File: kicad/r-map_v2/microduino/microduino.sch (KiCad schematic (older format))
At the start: 15 parts, among them P1 CONN_01X02, P2 CONN_RELE_BOARD, P3 CONN_01X05, P4 CONFIG, P5 USB_OTG, U1 Microduino, U2 ESDA6V1-5SC6, U3 LP2985LV, U4 TMP275

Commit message: Add files from last commit on sourceforge
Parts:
- removed R1: 1K0, w_smd_resistors:r_1206, symbol R
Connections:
- net GND: now also U4.5 (A2)
- net SCL: now reaches P3.2 (P2), U1.12 (A5), U2.5 (IO4), U4.2 (SCL)
- net SDA: now reaches P3.3 (P3), U1.13 (A4), U2.4 (IO3), U4.1 (SDA)
- net SCK: now reaches U1.19 (D13)
- net MISO: now reaches U1.20 (D12)
- net MOSI: now reaches U1.21 (D11)
- net CS-NRF24: now reaches U1.22 (D10)
- net CE-NRF24: now reaches U1.23 (D9)
- net CS-ENC28J60: now reaches P4.2 (P2), U1.24 (D8)
- net +3.3V: now reaches C3.1, D1.2 (A), P3.5 (P5), U1.26 (3V3), U3.5 (VOUT), U4.8 (Vcc)
- net +5V: now reaches C1.1, P1.1 (P1), P2.6 (P6), P3.1 (P1), P5.1 (VCC), U1.27 (5V), U3.1 (VIN), U3.3 (ON/OFF)
- net TX1: now reaches P2.4 (P4), U1.6 (D3)
- net INT-28J60: now reaches P2.5 (P5), U1.7 (D2)
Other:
- moved on the sheet: P4
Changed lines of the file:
@@
 	-1   0    0    1
 $EndComp
-Text Label 6950 4300 1    60   ~ 0
+Text Label 7150 4250 1    60   ~ 0
 GND
-Text Label 3600 4650 2    60   ~ 0
+Text Label 3700 4500 2    60   ~ 0
 Vcc_RELE
 NoConn ~ 5050 5200
@@
 	1    0    0    -1
 $EndComp
-$Comp
-L R R1
-U 1 1 54900F55
-P 8300 3550
-F 0 "R1" V 8380 3550 40  0000 C CNN
-F 1 "1K0" V 8307 3551 40  0000 C CNN
-F 2 "w_smd_resistors:r_1206" V 8230 3550 30  0001 C CNN
-F 3 "" H 8300 3550 30  0000 C CNN
-	1    8300 3550
-	1    0    0    -1
-$EndComp
 NoConn ~ 8200 3450
 $Comp
 L CONN_02X01 P4
 U 1 1 54837A8A
-P 7000 4750
-F 0 "P4" H 7000 4600 50  0000 C CNN
-F 1 "CONFIG" H 7000 4650 50  0000 C CNN
-F 2 "w_pin_strip:pin_strip_2" H 7000 3550 60  0001 C CNN
-F 3 "" H 7000 3550 60  0000 C CNN
-	1    7000 4750
+P 7150 4750
+F 0 "P4" H 7150 4600 50  0000 C CNN
+F 1 "CONFIG" H 7150 4650 50  0000 C CNN
+F 2 "w_pin_strip:pin_strip_2" H 7150 3550 60  0001 C CNN
+F 3 "" H 7150 3550 60  0000 C CNN
+	1    7150 4750
 	0    1    1    0
 $EndComp
@@
 NoConn ~ 5050 4600
 Wire Wire Line
-	4100 5300 5050 5300
-Wire Wire Line
-	5950 3850 5400 3850
+	4100 5300 4800 5300
+Wire Wire Line
+	4800 5300 5050 5300
+Wire Wire Line
+	5950 3850 5650 3850
+Wire Wire Line
+	5650 3850 5400 3850
 Wire Wire Line
 	5650 3850 5650 4100
 Wire Wire Line
-	4200 3000 7000 3000
-Wire Wire Line
-	6150 2850 6150 3650
+	4200 3000 6050 3000
+Wire Wire Line
+	6050 3000 7150 3000
+Wire Wire Line
+	6150 2850 6150 2900
+Wire Wire Line
+	6150 2900 6150 3650
 Wire Wire Line
 	6600 5200 6600 3650
@@
 	6600 5400 6600 5300
 Wire Wire Line
-	3700 5400 6600 5400
+	3700 5400 4050 5400
+Wire Wire Line
+	4050 5400 6600 5400
 Wire Wire Line
 	3700 5400 3700 4500
@@
 	4100 4500 4100 4600
 Wire Wire Line
-	5950 2850 5950 3850
-Wire Wire Line
-	5850 3650 5850 2850
+	5950 2850 5950 3250
+Wire Wire Line
+	5950 3250 5950 3850
+Wire Wire Line
+	5850 3650 5850 3100
+Wire Wire Line
+	5850 3100 5850 2850
 Wire Wire Line
 	6050 3000 6050 2850
@@
 	5750 3450 6700 3450
 Wire Wire Line
-	6700 3450 6700 5300
+	6700 5300 6700 3450
 Connection ~ 6600 5300
 Wire Wire Line
 	6600 3650 6150 3650
 Wire Wire Line
-	5400 3650 5850 3650
+	5400 3650 5550 3650
+Wire Wire Line
+	5550 3650 5850 3650
 Connection ~ 5550 3650
 Connection ~ 5650 3850
@@
 	4050 7200 4050 6950
 Wire Wire Line
-	2750 7200 6550 7200
+	2750 7200 3250 7200
+Wire Wire Line
+	3250 7200 3700 7200
+Wire Wire Line
+	3700 7200 4050 7200
+Wire Wire Line
+	4050 7200 4450 7200
+Wire Wire Line
+	4450 7200 5450 7200
+Wire Wire Line
+	5450 7200 6350 7200
+Wire Wire Line
+	6350 7200 6550 7200
 Wire Wire Line
 	6550 7200 6550 6950
 Wire Wire Line
-	5450 7100 5450 7300
+	5450 7100 5450 7200
+Wire Wire Line
+	5450 7200 5450 7300
 Connection ~ 5450 7200
 Wire Wire Line
-	6550 5200 6550 6650
-Wire Wire Line
-	4050 5400 4050 6650
-Wire Wire Line
-	2750 6100 4650 6100
+	6550 5200 6550 6100
+Wire Wire Line
+	6550 6100 6550 6650
+Wire Wire Line
+	4050 5400 4050 6100
+Wire Wire Line
+	4050 6100 4050 6300
+Wire Wire Line
+	4050 6300 4050 6650
+Wire Wire Line
+	2750 6100 3250 6100
+Wire Wire Line
+	3250 6100 3700 6100
+Wire Wire Line
+	3700 6100 4050 6100
+Wire Wire Line
+	4050 6100 4650 6100
 Wire Wire Line
 	4050 6300 4650 6300
 Connection ~ 4050 6300
 Wire Wire Line
-	6250 6100 6550 6100
+	6250 6100 6350 6100
+Wire Wire Line
+	6350 6100 6550 6100
 Connection ~ 6550 5200
 Connection ~ 4050 7200
@@
 Connection ~ 5950 3250
 Wire Wire Line
-	7000 3000 7000 4500
-Wire Wire Line
-	8400 3950 7000 3950
+	7150 3000 7150 3950
+Wire Wire Line
+	7150 3950 7150 4500
+Wire Wire Line
+	8400 3950 7700 3950
+Wire Wire Line
+	7700 3950 7150 3950
 Connection ~ 6050 3000
 Wire Wire Line
@@
 	8200 3000 8400 3000
 Wire Wire Line
-	8400 3000 8400 3950
+	8400 3000 8400 3100
+Wire Wire Line
+	8400 3100 8400 3200
+Wire Wire Line
+	8400 3200 8400 3950
 Connection ~ 7700 3950
 Wire Wire Line
@@
 Connection ~ 8400 3100
 Wire Wire Line
-	8200 3200 8300 3200
-Wire Wire Line
-	8300 3200 8300 3400
-Wire Wire Line
-	6450 5000 7000 5000
-Connection ~ 7000 3950
+	8200 3200 8400 3200
+Wire Wire Line
+	6450 5000 7150 5000
+Connection ~ 7150 3950
 Connection ~ 4050 5400
 Wire Wire Line
@@
 Connection ~ 4800 5300
 Wire Wire Line
-	6450 5200 6600 5200
-Wire Wire Line
-	6700 5300 6450 5300
-Wire Wire Line
-	7700 3850 7700 4100
-Connection ~ 8300 3950
-Wire Wire Line
-	8300 3700 8300 3950
+	6450 5200 6550 5200
+Wire Wire Line
+	6550 5200 6600 5200
+Wire Wire Line
+	6450 5300 6600 5300
+Wire Wire Line
+	6600 5300 6700 5300
+Wire Wire Line
+	7700 3850 7700 3950
+Wire Wire Line
+	7700 3950 7700 4100
 NoConn ~ 2750 6400
 $Comp
@@
 	6350 7050 6350 7200
 Connection ~ 6350 7200
+Text Label 5650 3650 0    60   ~ 0
+SCL
+Text Label 5750 3850 0    60   ~ 0
+SDA
+Connection ~ 8400 3200
+Text Label 6700 2900 0    60   ~ 0
++3.3V
+Text Label 6350 3450 0    60   ~ 0
++5V
+Text Label 4350 6100 0    60   ~ 0
+VIN
+Text Label 6450 4500 0    60   ~ 0
+SCK
+Text Label 6450 4600 0    60   ~ 0
+MISO
+Text Label 6450 4700 0    60   ~ 0
+MOSI
+Text Label 6450 5000 0    60   ~ 0
+CS-ENC28J60
+Text Label 4250 4700 0    60   ~ 0
+INT-28J60
+Text Label 6450 4900 0    60   ~ 0
+CE-NRF24
+Text Label 6450 4800 0    60   ~ 0
+CS-NRF24
+Text Label 4800 4700 0    60   ~ 0
+RX1
+Text Label 4800 4800 0    60   ~ 0
+TX1
 $EndSCHEMATC

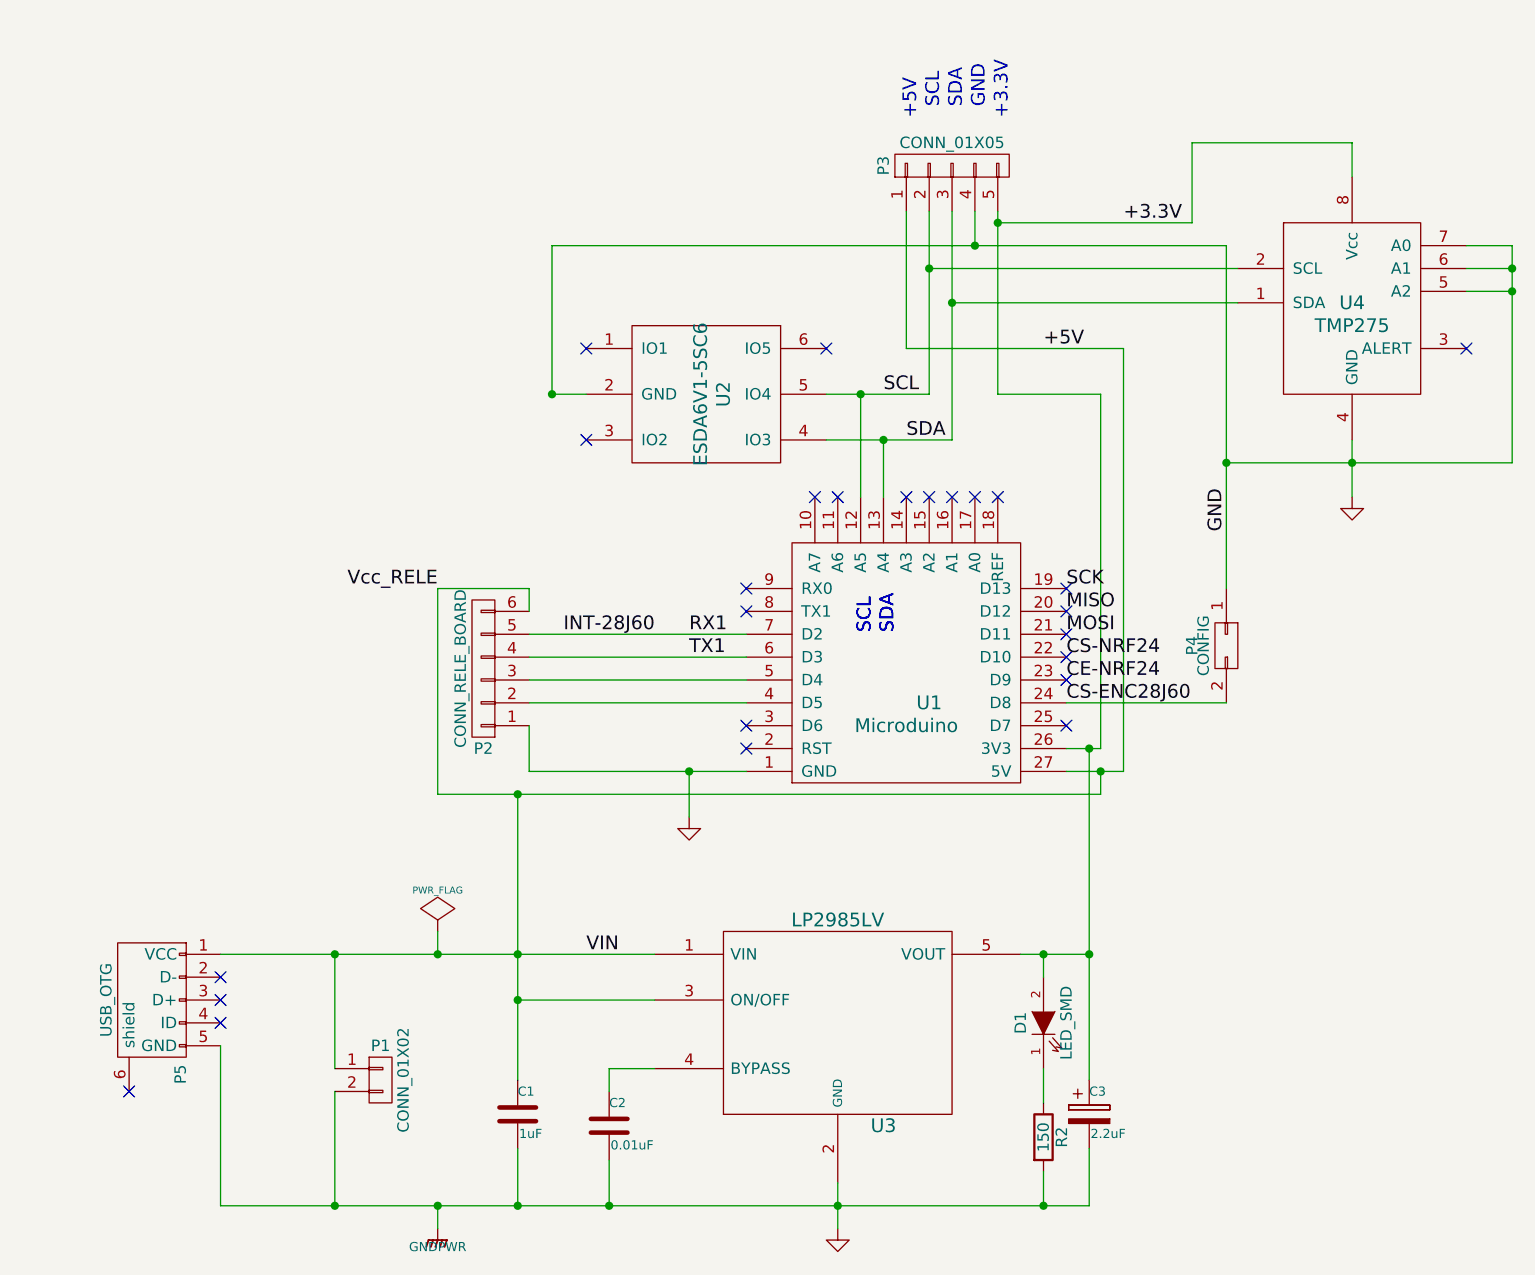
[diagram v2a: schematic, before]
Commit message: Modifiche a schema elettrico su modulo bluethoot, modificate connessioni per seriale 1. Modulo stima-i2c modificati pin per rele' e aggiunte connessioni esd su alimentazione. Rigenerati pcb.
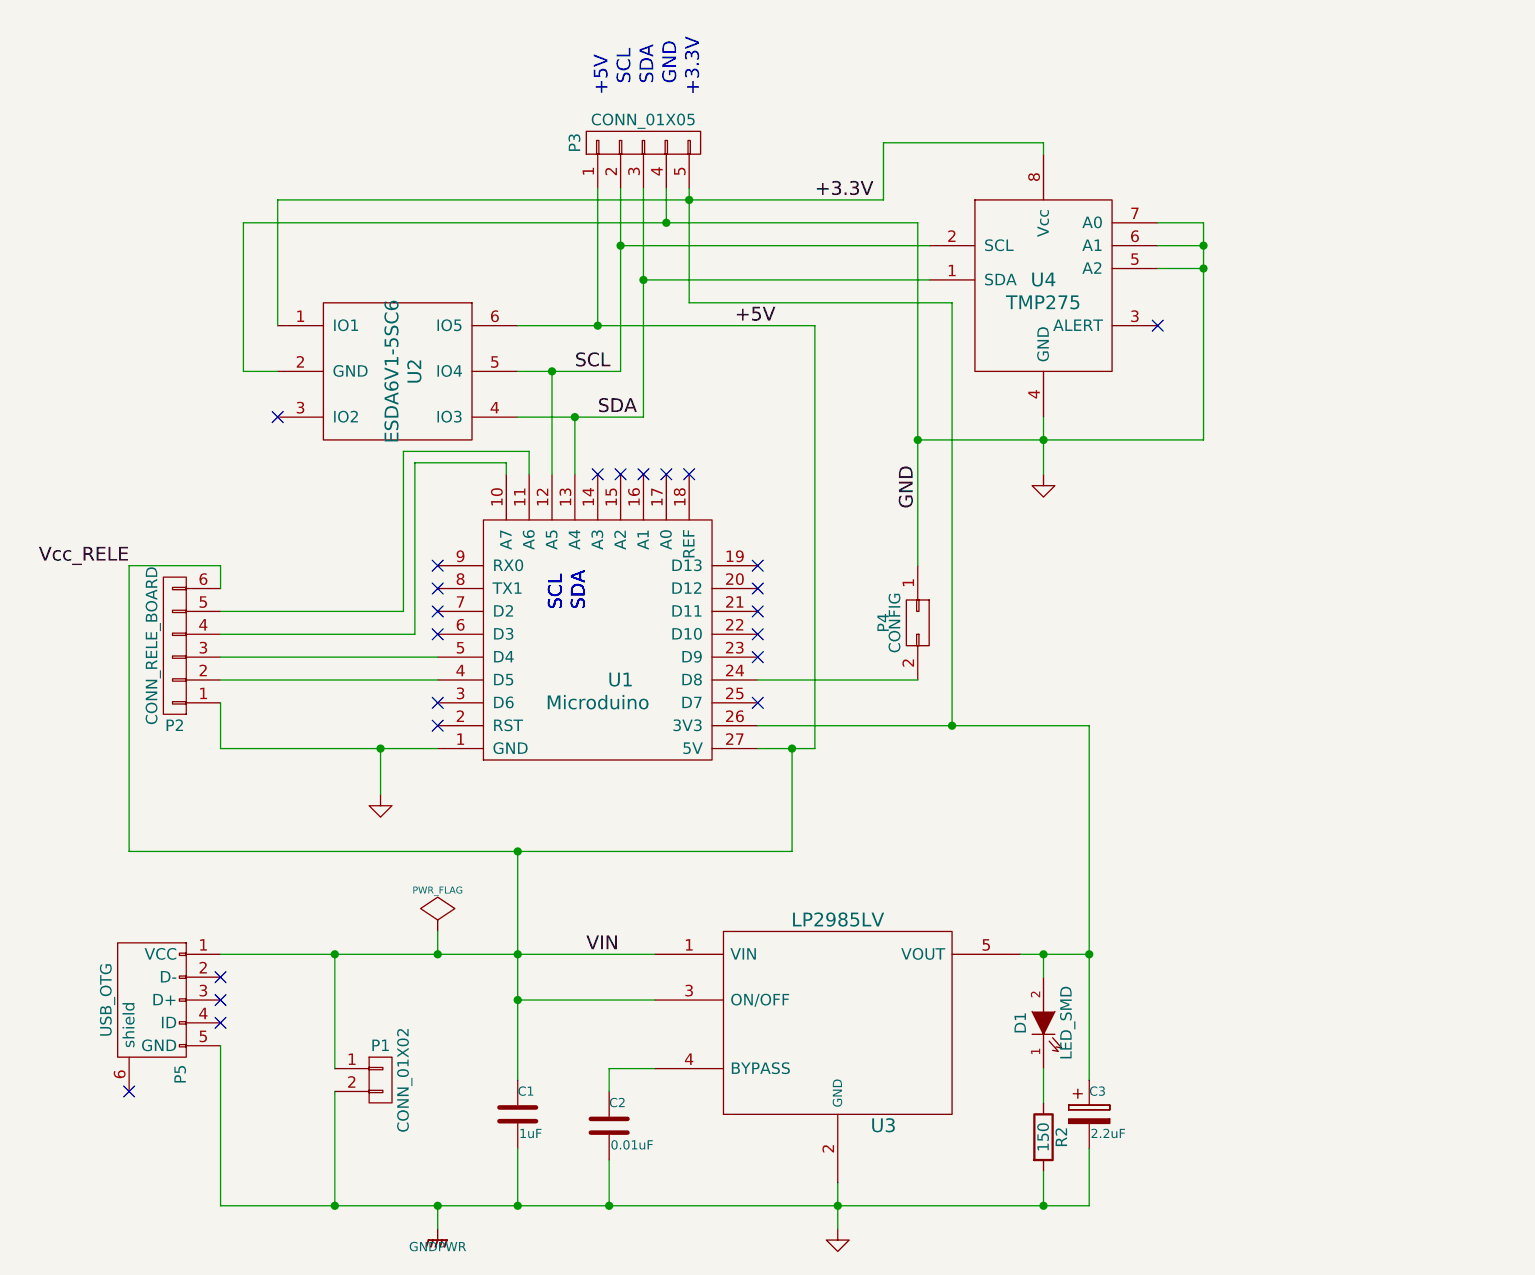
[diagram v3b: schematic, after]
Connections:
- net +3.3V: now also U2.1 (IO1)
- net +5V: now also U2.6 (IO5)
- net at U1.10 (A7): now also P2.4 (P4)
- net at U1.11 (A6): now also P2.5 (P5)
- net CE-NRF24: no longer names the net of U1.23 (D9)
- net CS-ENC28J60: no longer names the net of P4.2 (P2), U1.24 (D8)
- net CS-NRF24: no longer names the net of U1.22 (D10)
- net INT-28J60: no longer names the net of U1.7 (D2)
- net INT-28J60: no longer P2.5 (P5)
- net MISO: no longer names the net of U1.20 (D12)
- net MOSI: no longer names the net of U1.21 (D11)
- net SCK: no longer names the net of U1.19 (D13)
- net TX1: no longer names the net of U1.6 (D3)
- net TX1: no longer P2.4 (P4)
- no-connect marks 25 -> 23
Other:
- moved on the sheet: P2, P3, P4, U1, U2, U4
